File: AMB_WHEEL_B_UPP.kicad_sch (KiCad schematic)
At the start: 14 parts, among them U15 EPC2152, U16 EPC2152

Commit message: updated layouts, added motor
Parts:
- renumbered C111 to C135, C112 to C136, C113 to C137, C114 to C138, C115 to C139, C116 to C140, C117 to C141, C118 to C142, R79 to R135, R80 to R136, R81 to R137, R82 to R138, U15 to U13, U16 to U14

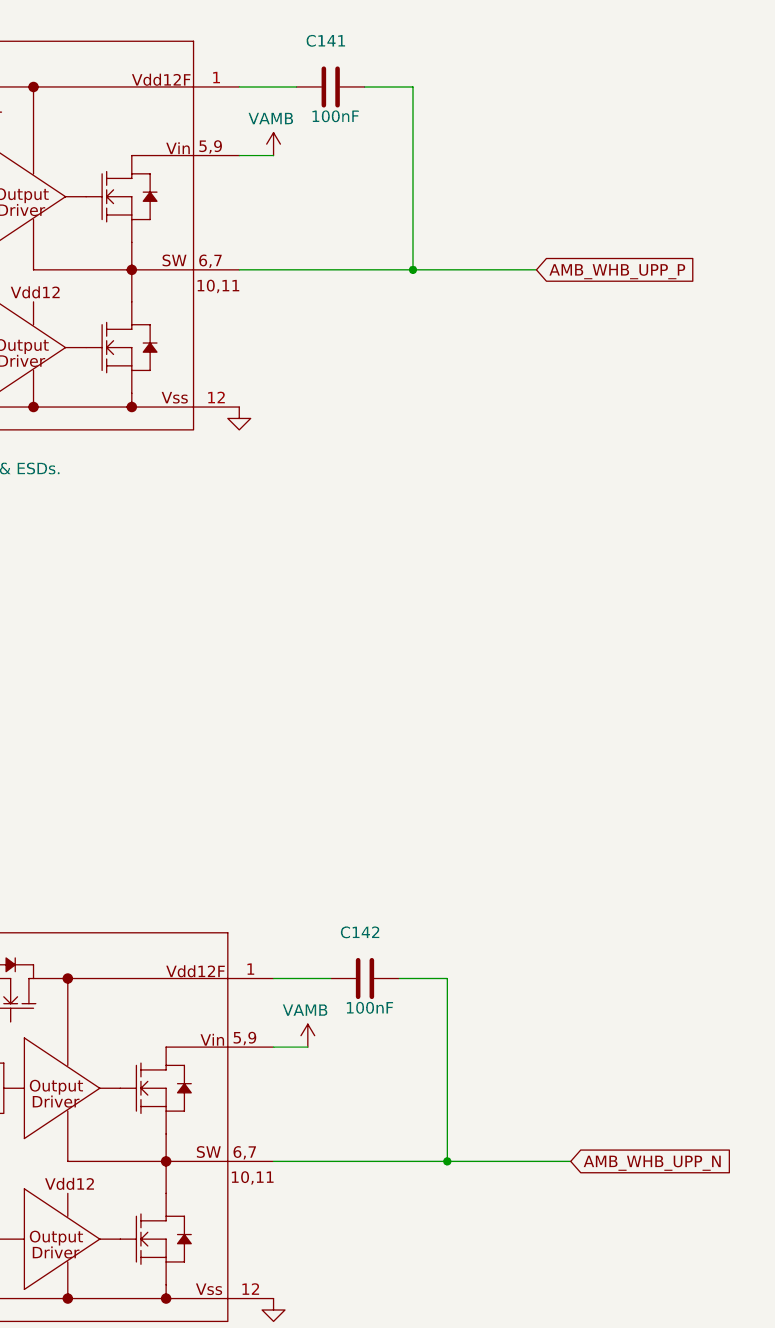
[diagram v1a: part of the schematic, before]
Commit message: Changes to layout pins
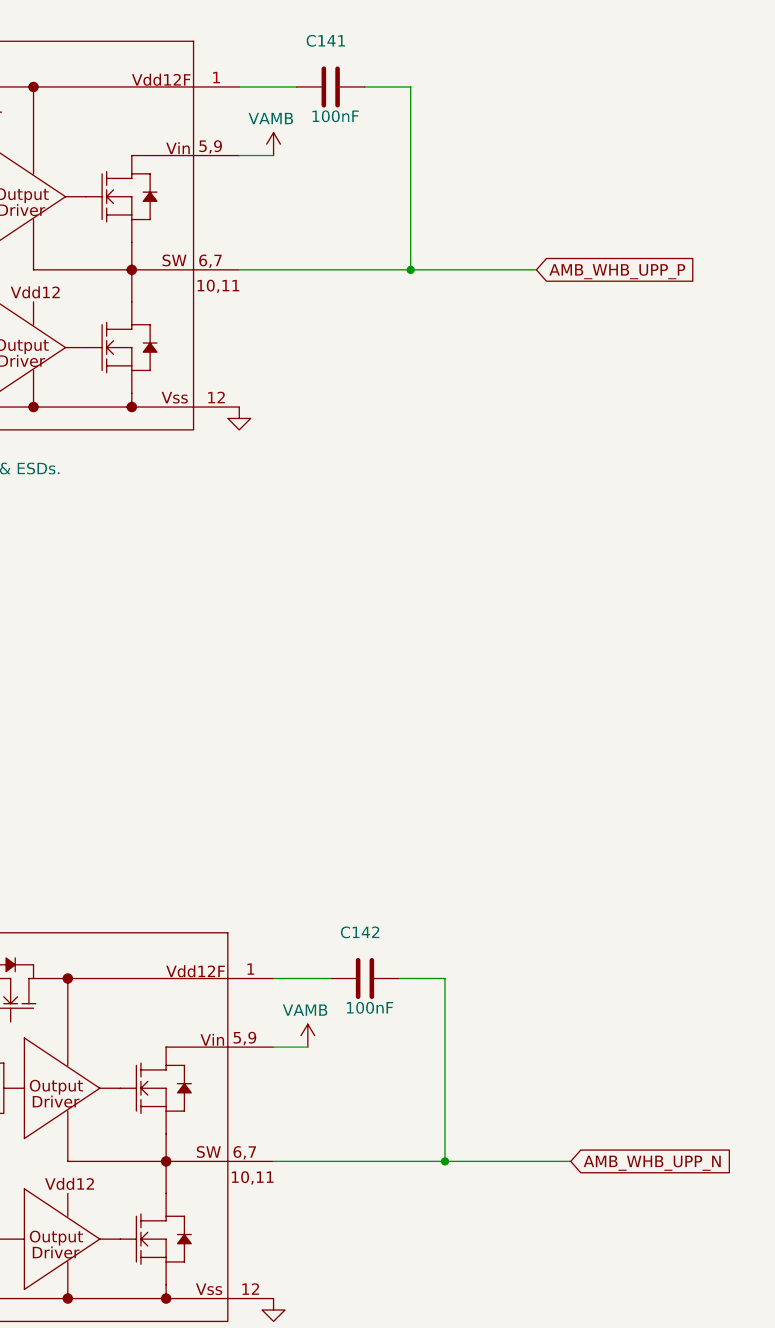
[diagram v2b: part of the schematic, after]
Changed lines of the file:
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@@
 	)
 	(junction
-		(at 192.024 158.75)
+		(at 191.77 158.75)
 		(diameter 0)
 		(color 0 0 0 0)
@@
 	)
 	(junction
-		(at 188.214 59.69)
+		(at 187.96 59.69)
 		(diameter 0)
 		(color 0 0 0 0)
@@
 	(wire
 		(pts
-			(xy 188.214 59.69) (xy 201.93 59.69)
+			(xy 187.96 59.69) (xy 201.93 59.69)
 		)
 		(stroke
@@
 	(wire
 		(pts
-			(xy 172.72 158.75) (xy 192.024 158.75)
+			(xy 172.72 158.75) (xy 191.77 158.75)
 		)
 		(stroke
@@
 	(wire
 		(pts
-			(xy 168.91 59.69) (xy 188.214 59.69)
+			(xy 168.91 59.69) (xy 187.96 59.69)
 		)
 		(stroke
@@
 	(wire
 		(pts
-			(xy 188.214 39.37) (xy 188.214 59.69)
+			(xy 187.96 39.37) (xy 187.96 59.69)
 		)
 		(stroke
@@
 	(wire
 		(pts
-			(xy 182.88 39.37) (xy 188.214 39.37)
+			(xy 182.88 39.37) (xy 187.96 39.37)
 		)
 		(stroke
@@
 	(wire
 		(pts
-			(xy 192.024 158.75) (xy 205.74 158.75)
+			(xy 191.77 158.75) (xy 205.74 158.75)
 		)
 		(stroke
@@
 	(wire
 		(pts
-			(xy 186.69 138.43) (xy 192.024 138.43)
+			(xy 186.69 138.43) (xy 191.77 138.43)
 		)
 		(stroke
@@
 	(wire
 		(pts
-			(xy 192.024 138.43) (xy 192.024 158.75)
+			(xy 191.77 138.43) (xy 191.77 158.75)
 		)
 		(stroke
@@
 	)
 	(symbol
-		(lib_id "CIAA_ACC:GND")
+		(lib_id "power:GND")
 		(at 168.91 74.93 0)
 		(unit 1)
@@
 		(property "Footprint" ""
 			(at 168.91 74.93 0)
+			(hide yes)
 			(show_name no)
 			(do_not_autoplace no)
@@
 		(property "Datasheet" ""
 			(at 168.91 74.93 0)
+			(hide yes)
 			(show_name no)
 			(do_not_autoplace no)
@@
 			)
 		)
-		(property "Description" ""
+		(property "Description" "Power symbol creates a global label with name \"GND\" , ground"
 			(at 168.91 74.93 0)
+			(hide yes)
 			(show_name no)
 			(do_not_autoplace no)
@@
 	)
 	(symbol
-		(lib_id "CIAA_ACC:GND")
+		(lib_id "power:GND")
 		(at 172.72 173.99 0)
 		(unit 1)
@@
 		(property "Footprint" ""
 			(at 172.72 173.99 0)
+			(hide yes)
 			(show_name no)
 			(do_not_autoplace no)
@@
 		(property "Datasheet" ""
 			(at 172.72 173.99 0)
+			(hide yes)
 			(show_name no)
 			(do_not_autoplace no)
@@
 			)
 		)
-		(property "Description" ""
+		(property "Description" "Power symbol creates a global label with name \"GND\" , ground"
 			(at 172.72 173.99 0)
+			(hide yes)
 			(show_name no)
 			(do_not_autoplace no)
@@
 	)
 	(symbol
-		(lib_id "CIAA_ACC:GND")
+		(lib_id "power:GND")
 		(at 106.68 147.32 0)
 		(unit 1)
@@
 		(property "Footprint" ""
 			(at 106.68 147.32 0)
+			(hide yes)
 			(show_name no)
 			(do_not_autoplace no)
@@
 		(property "Datasheet" ""
 			(at 106.68 147.32 0)
+			(hide yes)
 			(show_name no)
 			(do_not_autoplace no)
@@
 			)
 		)
-		(property "Description" ""
+		(property "Description" "Power symbol creates a global label with name \"GND\" , ground"
 			(at 106.68 147.32 0)
+			(hide yes)
 			(show_name no)
 			(do_not_autoplace no)
@@
 	)
 	(symbol
-		(lib_id "CIAA_ACC:GND")
+		(lib_id "power:GND")
 		(at 111.76 173.99 0)
 		(unit 1)
@@
 		(property "Footprint" ""
 			(at 111.76 173.99 0)
+			(hide yes)
 			(show_name no)
 			(do_not_autoplace no)
@@
 		(property "Datasheet" ""
 			(at 111.76 173.99 0)
+			(hide yes)
 			(show_name no)
 			(do_not_autoplace no)
@@
 			)
 		)
-		(property "Description" ""
+		(property "Description" "Power symbol creates a global label with name \"GND\" , ground"
 			(at 111.76 173.99 0)
+			(hide yes)
 			(show_name no)
 			(do_not_autoplace no)
@@
 	)
 	(symbol
-		(lib_id "CIAA_ACC:GND")
+		(lib_id "power:GND")
 		(at 102.87 48.26 0)
 		(unit 1)
@@
 		(property "Footprint" ""
 			(at 102.87 48.26 0)
+			(hide yes)
 			(show_name no)
 			(do_not_autoplace no)
@@
 		(property "Datasheet" ""
 			(at 102.87 48.26 0)
+			(hide yes)
 			(show_name no)
 			(do_not_autoplace no)
@@
 			)
 		)
-		(property "Description" ""
+		(property "Description" "Power symbol creates a global label with name \"GND\" , ground"
 			(at 102.87 48.26 0)
+			(hide yes)
 			(show_name no)
 			(do_not_autoplace no)
@@
 	)
 	(symbol
-		(lib_id "CIAA_ACC:GND")
+		(lib_id "power:GND")
 		(at 80.01 58.42 0)
 		(unit 1)
@@
 		(property "Footprint" ""
 			(at 80.01 58.42 0)
+			(hide yes)
 			(show_name no)
 			(do_not_autoplace no)
@@
 		(property "Datasheet" ""
 			(at 80.01 58.42 0)
+			(hide yes)
 			(show_name no)
 			(do_not_autoplace no)
@@
 			)
 		)
-		(property "Description" ""
+		(property "Description" "Power symbol creates a global label with name \"GND\" , ground"
 			(at 80.01 58.42 0)
+			(hide yes)
 			(show_name no)
 			(do_not_autoplace no)
@@
 	)
 	(symbol
-		(lib_id "CIAA_ACC:GND")
+		(lib_id "power:GND")
 		(at 83.82 157.48 0)
 		(unit 1)
@@
 		(property "Footprint" ""
 			(at 83.82 157.48 0)
+			(hide yes)
 			(show_name no)
 			(do_not_autoplace no)
@@
 		(property "Datasheet" ""
 			(at 83.82 157.48 0)
+			(hide yes)
 			(show_name no)
 			(do_not_autoplace no)
@@
 			)
 		)
-		(property "Description" ""
+		(property "Description" "Power symbol creates a global label with name \"GND\" , ground"
 			(at 83.82 157.48 0)
+			(hide yes)
 			(show_name no)
 			(do_not_autoplace no)
@@
 	)
 	(symbol
-		(lib_id "CIAA_ACC:GND")
+		(lib_id "power:GND")
 		(at 50.8 106.68 0)
 		(unit 1)
@@
 		(property "Footprint" ""
 			(at 50.8 106.68 0)
+			(hide yes)
 			(show_name no)
 			(do_not_autoplace no)
@@
 		(property "Datasheet" ""
 			(at 50.8 106.68 0)
+			(hide yes)
 			(show_name no)
 			(do_not_autoplace no)
@@
 			)
 		)
-		(property "Description" ""
+		(property "Description" "Power symbol creates a global label with name \"GND\" , ground"
 			(at 50.8 106.68 0)
+			(hide yes)
 			(show_name no)
 			(do_not_autoplace no)
@@
 	)
 	(symbol
-		(lib_id "CIAA_ACC:GND")
+		(lib_id "power:GND")
 		(at 107.95 74.93 0)
 		(unit 1)
@@
 		(property "Footprint" ""
 			(at 107.95 74.93 0)
+			(hide yes)
 			(show_name no)
 			(do_not_autoplace no)
@@
 		(property "Datasheet" ""
 			(at 107.95 74.93 0)
+			(hide yes)
 			(show_name no)
 			(do_not_autoplace no)
@@
 			)
 		)
-		(property "Description" ""
+		(property "Description" "Power symbol creates a global label with name \"GND\" , ground"
 			(at 107.95 74.93 0)
+			(hide yes)
 			(show_name no)
 			(do_not_autoplace no)
@@
 	)
 	(symbol
-		(lib_id "CIAA_ACC:GND")
+		(lib_id "power:GND")
 		(at 80.01 172.72 0)
 		(unit 1)
@@
 		(property "Footprint" ""
 			(at 80.01 172.72 0)
+			(hide yes)
 			(show_name no)
 			(do_not_autoplace no)
@@
 		(property "Datasheet" ""
 			(at 80.01 172.72 0)
+			(hide yes)
 			(show_name no)
 			(do_not_autoplace no)
@@
 			)
 		)
-		(property "Description" ""
+		(property "Description" "Power symbol creates a global label with name \"GND\" , ground"
 			(at 80.01 172.72 0)
+			(hide yes)
 			(show_name no)
 			(do_not_autoplace no)
@@
 	)
 	(symbol
-		(lib_id "CIAA_ACC:GND")
+		(lib_id "power:GND")
 		(at 76.2 73.66 0)
 		(unit 1)
@@
 		(property "Footprint" ""
 			(at 76.2 73.66 0)
+			(hide yes)
 			(show_name no)
 			(do_not_autoplace no)
@@
 		(property "Datasheet" ""
 			(at 76.2 73.66 0)
+			(hide yes)
 			(show_name no)
 			(do_not_autoplace no)
@@
 			)
 		)
-		(property "Description" ""
+		(property "Description" "Power symbol creates a global label with name \"GND\" , ground"
 			(at 76.2 73.66 0)
+			(hide yes)
 			(show_name no)
 			(do_not_autoplace no)
